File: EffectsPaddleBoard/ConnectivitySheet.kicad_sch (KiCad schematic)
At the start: 1 part, among them U2 FT2232HL

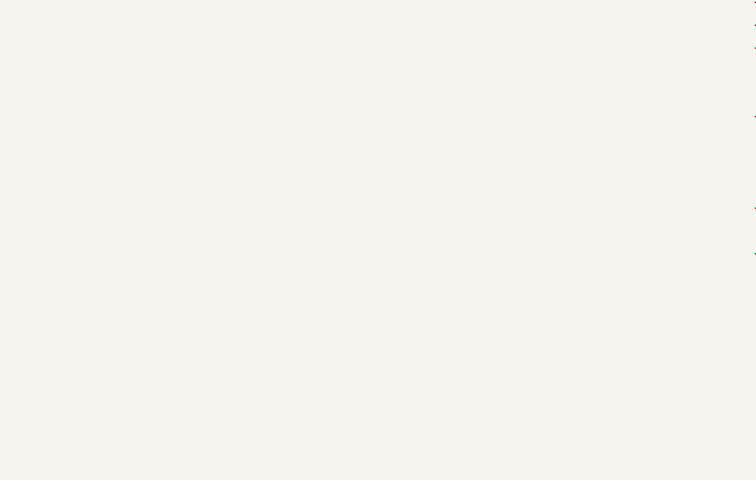
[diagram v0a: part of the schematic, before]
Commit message: Added power to uC, but overall power not finished
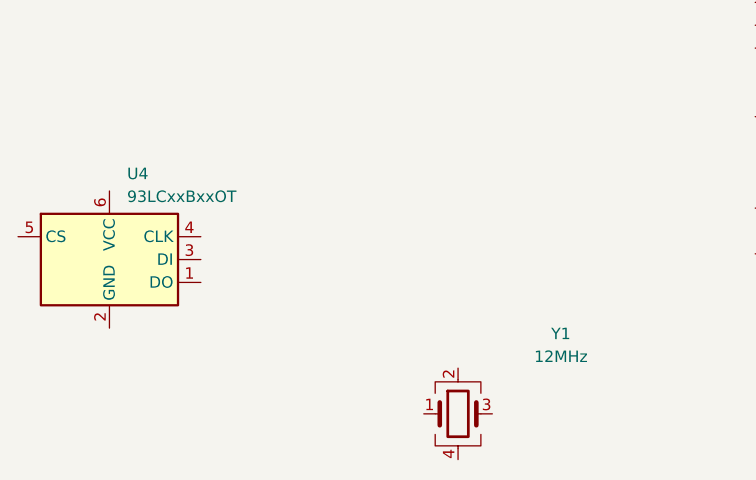
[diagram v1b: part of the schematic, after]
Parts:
- added U4: 93LCxxBxxOT, Package_TO_SOT_SMD:SOT-23-6, symbol Memory_EEPROM:93LCxxBxxOT
- added Y1: 12MHz, symbol Device:Crystal_GND24
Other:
- company: (none) -> Selbstständig
- title: (none) -> Effects Paddle
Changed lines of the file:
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@@
 (kicad_sch (version 20230121) (generator eeschema)
   (paper "A4")
+  (title_block
+    (title "Effects Paddle")
+    (date "2023-07-01")
+    (rev "0.1")
+    (company "Selbstständig")
+  )
   (symbol (lib_id "Interface_USB:FT2232HL") (at 148.59 96.52 0) (unit 1)
     (in_bom yes) (on_board yes) (dnp no) (fields_autoplaced)
@@
         )
       )
+    )
+  )
+  (symbol (lib_id "Device:Crystal_GND24") (at 85.09 160.02 0) (unit 1)
+    (in_bom yes) (on_board yes) (dnp no)
+    (property "Reference" "Y1" (at 96.52 151.13 0)
+      (effects (font (size 1.27 1.27)))
+    )
+    (property "Value" "12MHz" (at 96.52 153.67 0)
+      (effects (font (size 1.27 1.27)))
+    )
+    (property "Footprint" "" (at 85.09 160.02 0)
+      (effects (font (size 1.27 1.27)) hide)
+    )
+    (property "Datasheet" "~" (at 85.09 160.02 0)
+      (effects (font (size 1.27 1.27)) hide)
+    )
+    (pin "1")
+    (pin "2")
+    (pin "3")
+    (pin "4")
+    (instances
+      (project "EffectsPaddleBoard"
+        (path "/40bb1606-5207-4492-95b9-876879aab2b4/430de8a6-c174-447f-a683-0bfbe392d7bf"
+          (reference "Y1") (unit 1)
+        )
+        (path "/40bb1606-5207-4492-95b9-876879aab2b4/f12e44f9-f182-4a4e-be12-78ee397dee5a"
+          (reference "Y2") (unit 1)
+        )
+      )
+    )
+  )
+  (symbol (lib_id "Memory_EEPROM:93LCxxBxxOT") (at 46.355 142.875 0) (unit 1)
+    (in_bom yes) (on_board yes) (dnp no) (fields_autoplaced)
+    (property "Reference" "U4" (at 48.3109 133.35 0)
+      (effects (font (size 1.27 1.27)) (justify left))
+    )
+    (property "Value" "93LCxxBxxOT" (at 48.3109 135.89 0)
+      (effects (font (size 1.27 1.27)) (justify left))
+    )
+    (property "Footprint" "Package_TO_SOT_SMD:SOT-23-6" (at 46.355 142.875 0)
+      (effects (font (size 1.27 1.27)) hide)
+    )
+    (property "Datasheet" "http://ww1.microchip.com/downloads/en/DeviceDoc/20001749K.pdf" (at 46.355 142.875 0)
+      (effects (font (size 1.27 1.27)) hide)
+    )
+    (pin "1")
+    (pin "2")
+    (pin "3")
+    (pin "4")
+    (pin "5")
+    (pin "6")
+    (instances
+      (project "EffectsPaddleBoard"
+        (path "/40bb1606-5207-4492-95b9-876879aab2b4/f12e44f9-f182-4a4e-be12-78ee397dee5a"
+          (reference "U4") (unit 1)
+        )
+      )
